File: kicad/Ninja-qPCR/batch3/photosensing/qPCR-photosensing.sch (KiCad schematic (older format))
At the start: 26 parts, among them J2 Conn_01x02_Male, J3 Conn_01x05_Male, J4 Conn_01x05_Male, U2 ADS1219IPWR

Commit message: wire xtal
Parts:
- R? (x2): value R -> ?
- Y?: value Crystal -> 32.768kHz?
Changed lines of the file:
@@
 P 4650 6000
 F 0 "R?" V 4443 6000 50  0000 C CNN
-F 1 "R" V 4534 6000 50  0000 C CNN
+F 1 "?" V 4534 6000 50  0000 C CNN
 F 2 "" V 4580 6000 50  0001 C CNN
 F 3 "~" H 4650 6000 50  0001 C CNN
@@
 P 5050 6250
 F 0 "R?" H 5120 6296 50  0000 L CNN
-F 1 "R" H 5120 6205 50  0000 L CNN
+F 1 "?" H 5120 6205 50  0000 L CNN
 F 2 "" V 4980 6250 50  0001 C CNN
 F 3 "~" H 5050 6250 50  0001 C CNN
@@
 P 4650 6500
 F 0 "Y?" H 4650 6768 50  0000 C CNN
-F 1 "Crystal" H 4650 6677 50  0000 C CNN
+F 1 "32.768kHz?" H 4650 6677 50  0000 C CNN
 F 2 "" H 4650 6500 50  0001 C CNN
 F 3 "~" H 4650 6500 50  0001 C CNN

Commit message: wire xtal
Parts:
- C? (x2): value C -> ?
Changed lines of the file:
@@
 P 4300 6750
 F 0 "C?" H 4415 6796 50  0000 L CNN
-F 1 "C" H 4415 6705 50  0000 L CNN
+F 1 "?" H 4415 6705 50  0000 L CNN
 F 2 "" H 4338 6600 50  0001 C CNN
 F 3 "~" H 4300 6750 50  0001 C CNN
@@
 P 5050 6750
 F 0 "C?" H 5165 6796 50  0000 L CNN
-F 1 "C" H 5165 6705 50  0000 L CNN
+F 1 "?" H 5165 6705 50  0000 L CNN
 F 2 "" H 5088 6600 50  0001 C CNN
 F 3 "~" H 5050 6750 50  0001 C CNN

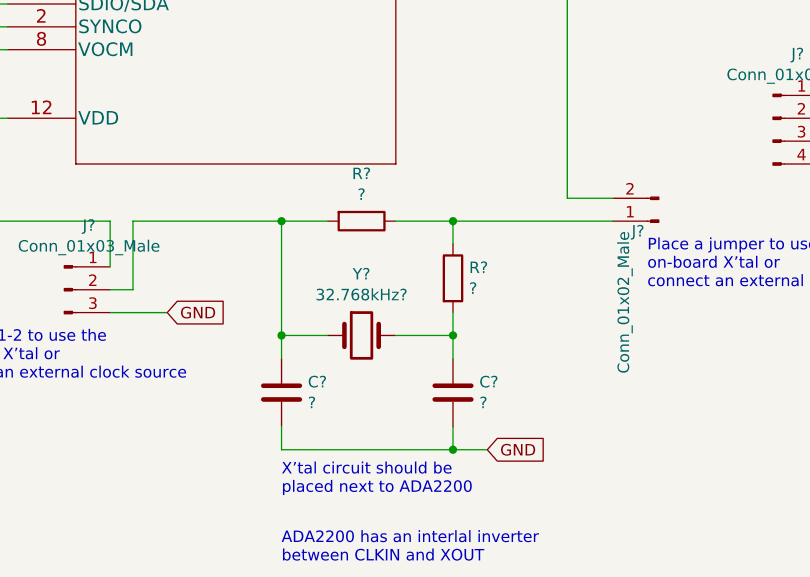
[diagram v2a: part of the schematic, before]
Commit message: change 20M to 10M+10M
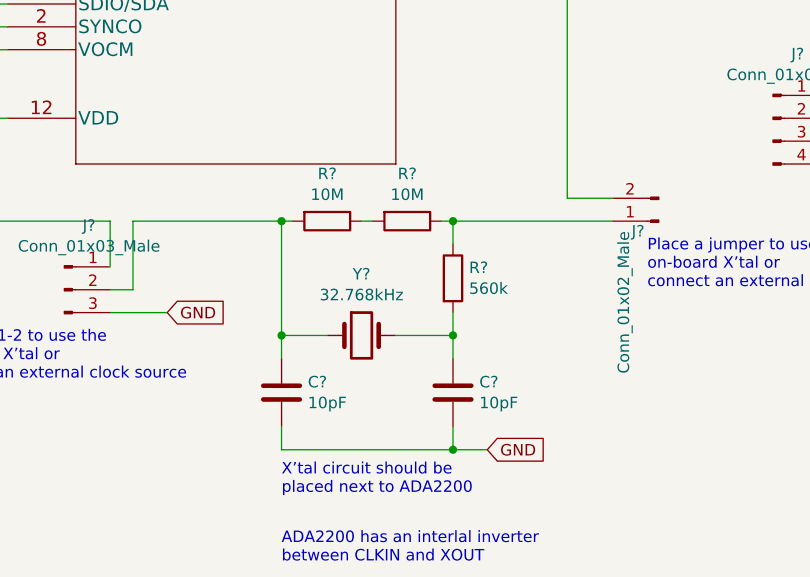
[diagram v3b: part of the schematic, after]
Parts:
- added R?: 10M, symbol Device:R
- C? (x2): value ? -> 10pF
- R?: value ? -> 10M
- R?: value ? -> 560k
- Y?: value 32.768kHz? -> 32.768kHz
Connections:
- net at J?.1 (Pin_1), R?.1: now also R?.1; no longer R?.1
- new net: R?.1, R?.2
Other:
- moved on the sheet: R?
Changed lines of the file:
@@
 L Device:R R?
 U 1 1 5FE4E4E3
-P 4650 6000
-F 0 "R?" V 4443 6000 50  0000 C CNN
-F 1 "?" V 4534 6000 50  0000 C CNN
-F 2 "" V 4580 6000 50  0001 C CNN
-F 3 "~" H 4650 6000 50  0001 C CNN
-	1    4650 6000
-	0    1    1    0
-$EndComp
-Wire Wire Line
-	4800 6000 5050 6000
-Wire Wire Line
-	4500 6000 4300 6000
+P 4500 6000
+F 0 "R?" V 4293 6000 50  0000 C CNN
+F 1 "10M" V 4384 6000 50  0000 C CNN
+F 2 "" V 4430 6000 50  0001 C CNN
+F 3 "~" H 4500 6000 50  0001 C CNN
+	1    4500 6000
+	0    1    1    0
+$EndComp
 $Comp
 L Device:R R?
@@
 P 5050 6250
 F 0 "R?" H 5120 6296 50  0000 L CNN
-F 1 "?" H 5120 6205 50  0000 L CNN
+F 1 "560k" H 5120 6205 50  0000 L CNN
 F 2 "" V 4980 6250 50  0001 C CNN
 F 3 "~" H 5050 6250 50  0001 C CNN
@@
 Wire Wire Line
 	5050 6100 5050 6000
-Connection ~ 5050 6000
 $Comp
 L Device:Crystal Y?
@@
 P 4650 6500
 F 0 "Y?" H 4650 6768 50  0000 C CNN
-F 1 "32.768kHz?" H 4650 6677 50  0000 C CNN
+F 1 "32.768kHz" H 4650 6677 50  0000 C CNN
 F 2 "" H 4650 6500 50  0001 C CNN
 F 3 "~" H 4650 6500 50  0001 C CNN
@@
 P 4300 6750
 F 0 "C?" H 4415 6796 50  0000 L CNN
-F 1 "?" H 4415 6705 50  0000 L CNN
+F 1 "10pF" H 4415 6705 50  0000 L CNN
 F 2 "" H 4338 6600 50  0001 C CNN
 F 3 "~" H 4300 6750 50  0001 C CNN
@@
 P 5050 6750
 F 0 "C?" H 5165 6796 50  0000 L CNN
-F 1 "?" H 5165 6705 50  0000 L CNN
+F 1 "10pF" H 5165 6705 50  0000 L CNN
 F 2 "" H 5088 6600 50  0001 C CNN
 F 3 "~" H 5050 6750 50  0001 C CNN
@@
 Wire Wire Line
 	3650 6000 4300 6000
-Connection ~ 4300 6000
 Wire Wire Line
 	3550 6000 2300 6000
@@
 Text Notes 6600 950  0    50   ~ 0
 SMALL GAIN FOR\nSTRONG SIGNAL
+$Comp
+L Device:R R?
+U 1 1 5FF71CFB
+P 4850 6000
+F 0 "R?" V 4643 6000 50  0000 C CNN
+F 1 "10M" V 4734 6000 50  0000 C CNN
+F 2 "" V 4780 6000 50  0001 C CNN
+F 3 "~" H 4850 6000 50  0001 C CNN
+	1    4850 6000
+	0    1    1    0
+$EndComp
+Wire Wire Line
+	5050 6000 5000 6000
+Connection ~ 5050 6000
+Wire Wire Line
+	4700 6000 4650 6000
+Wire Wire Line
+	4350 6000 4300 6000
+Connection ~ 4300 6000
 $EndSCHEMATC

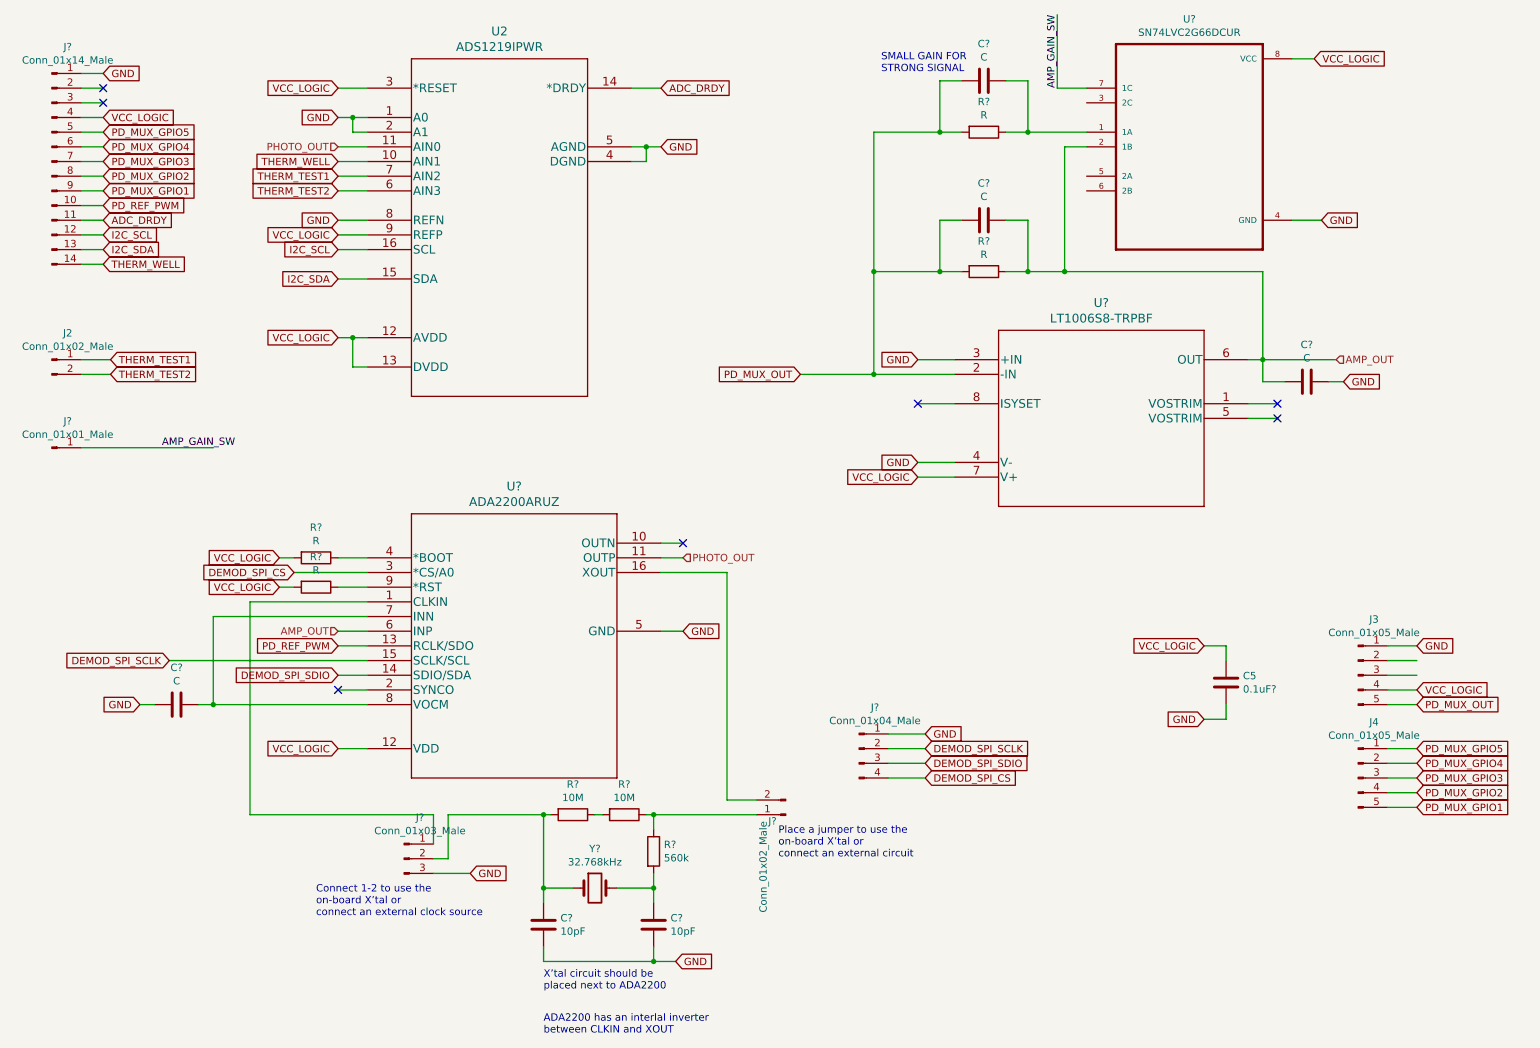
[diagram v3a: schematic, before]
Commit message: Updated values of resistor & capacitors of photosensing board
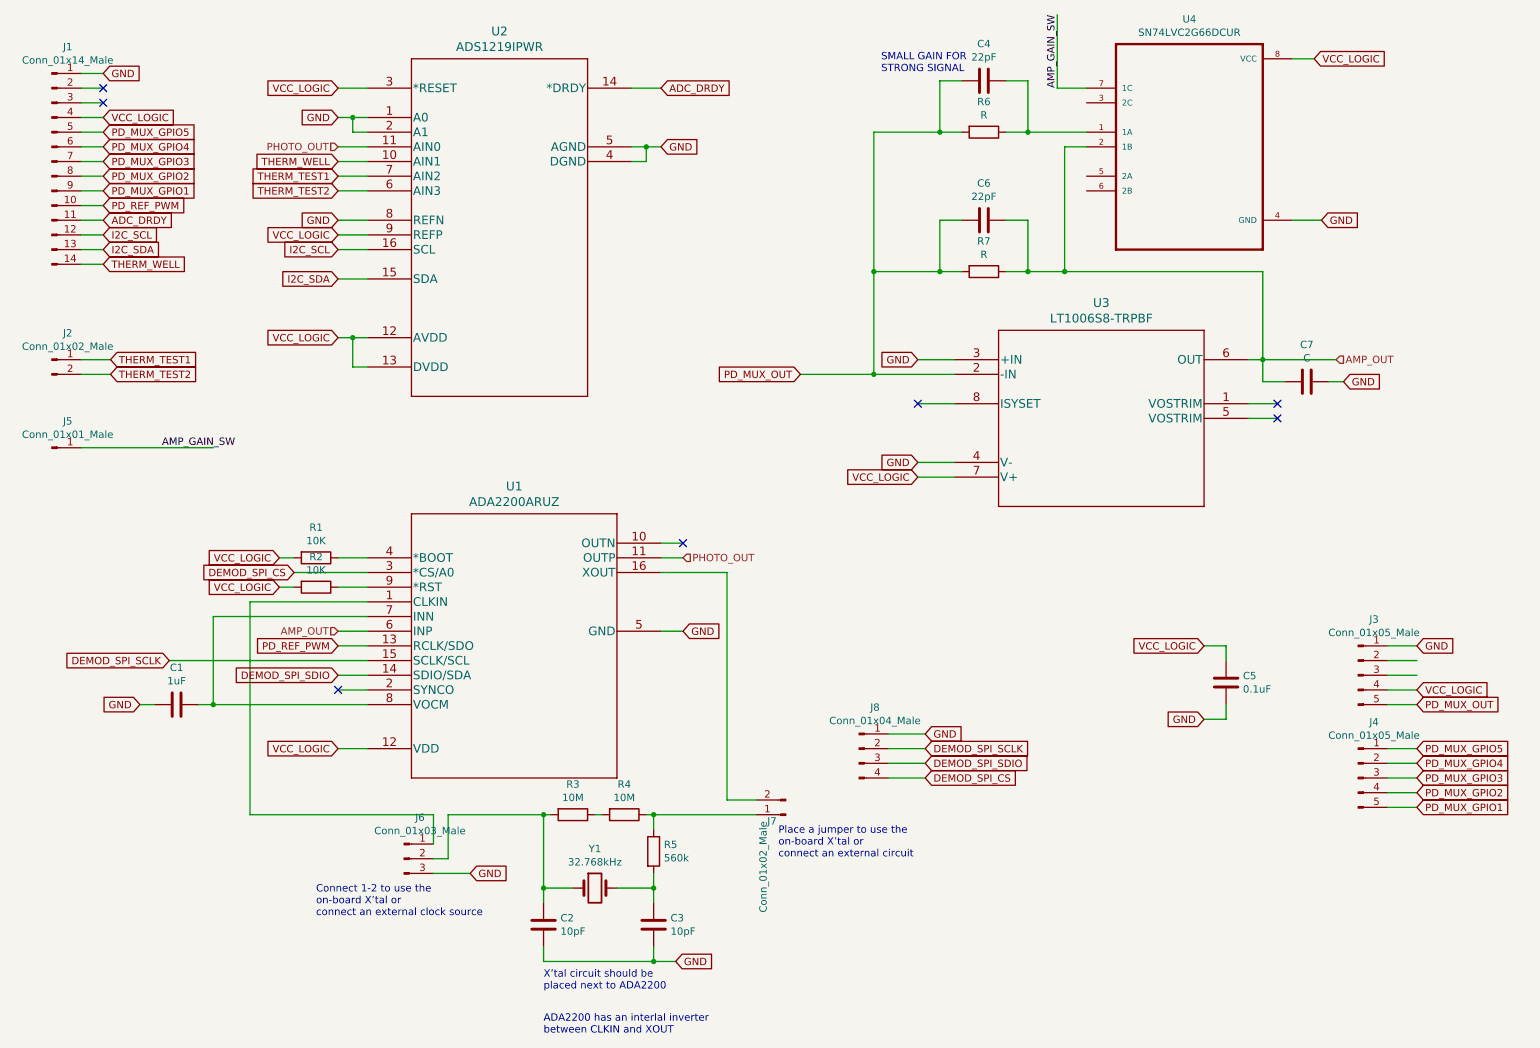
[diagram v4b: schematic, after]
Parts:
- C1: renamed from C?; value C -> 1uF
- C4, C6: renamed from C?; value C -> 22pF
- C5: value 0.1uF? -> 0.1uF
- R1, R2: renamed from R?; value R -> 10K
- gave numbers to parts that had none: 17
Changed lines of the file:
@@
 P 8950 5100
 F 0 "C5" H 9065 5146 50  0000 L CNN
-F 1 "0.1uF?" H 9065 5055 50  0000 L CNN
+F 1 "0.1uF" H 9065 5055 50  0000 L CNN
 F 2 "Capacitors_SMD:C_0805_HandSoldering" H 8988 4950 50  0001 C CNN
 F 3 "~" H 8950 5100 50  0001 C CNN
@@
 	2900 4850 3100 4850
 $Comp
-L Ninja-qPCR:ADA2200ARUZ U?
+L Ninja-qPCR:ADA2200ARUZ U1
 U 1 1 5F7FB45A
 P 3100 4250
-F 0 "U?" H 4100 4737 60  0000 C CNN
+F 0 "U1" H 4100 4737 60  0000 C CNN
 F 1 "ADA2200ARUZ" H 4100 4631 60  0000 C CNN
 F 2 "RU_16_ADI" H 4100 4590 60  0001 C CNN
@@
 $EndComp
 $Comp
-L Device:R R?
+L Device:R R1
 U 1 1 5FDD9D62
 P 2750 4250
-F 0 "R?" V 2543 4250 50  0000 C CNN
-F 1 "R" V 2634 4250 50  0000 C CNN
+F 0 "R1" V 2543 4250 50  0000 C CNN
+F 1 "10K" V 2634 4250 50  0000 C CNN
 F 2 "" V 2680 4250 50  0001 C CNN
 F 3 "~" H 2750 4250 50  0001 C CNN
@@
 $EndComp
 $Comp
-L Device:R R?
+L Device:R R2
 U 1 1 5FDDE2F4
 P 2750 4450
-F 0 "R?" V 2543 4450 50  0000 C CNN
-F 1 "R" V 2634 4450 50  0000 C CNN
+F 0 "R2" V 2543 4450 50  0000 C CNN
+F 1 "10K" V 2634 4450 50  0000 C CNN
 F 2 "" V 2680 4450 50  0001 C CNN
 F 3 "~" H 2750 4450 50  0001 C CNN
@@
 	5100 4350 5550 4350
 $Comp
-L Device:R R?
+L Device:R R3
 U 1 1 5FE4E4E3
 P 4500 6000
-F 0 "R?" V 4293 6000 50  0000 C CNN
+F 0 "R3" V 4293 6000 50  0000 C CNN
 F 1 "10M" V 4384 6000 50  0000 C CNN
 F 2 "" V 4430 6000 50  0001 C CNN
@@
 $EndComp
 $Comp
-L Device:R R?
+L Device:R R5
 U 1 1 5FE5F208
 P 5050 6250
-F 0 "R?" H 5120 6296 50  0000 L CNN
+F 0 "R5" H 5120 6296 50  0000 L CNN
 F 1 "560k" H 5120 6205 50  0000 L CNN
 F 2 "" V 4980 6250 50  0001 C CNN
@@
 	5050 6100 5050 6000
 $Comp
-L Device:Crystal Y?
+L Device:Crystal Y1
 U 1 1 5FE652B7
 P 4650 6500
-F 0 "Y?" H 4650 6768 50  0000 C CNN
+F 0 "Y1" H 4650 6768 50  0000 C CNN
 F 1 "32.768kHz" H 4650 6677 50  0000 C CNN
 F 2 "" H 4650 6500 50  0001 C CNN
@@
 	4300 6500 4300 6000
 $Comp
-L Device:C C?
+L Device:C C2
 U 1 1 5FE71967
 P 4300 6750
-F 0 "C?" H 4415 6796 50  0000 L CNN
+F 0 "C2" H 4415 6796 50  0000 L CNN
 F 1 "10pF" H 4415 6705 50  0000 L CNN
 F 2 "" H 4338 6600 50  0001 C CNN
@@
 $EndComp
 $Comp
-L Device:C C?
+L Device:C C3
 U 1 1 5FE721BD
 P 5050 6750
-F 0 "C?" H 5165 6796 50  0000 L CNN
+F 0 "C3" H 5165 6796 50  0000 L CNN
 F 1 "10pF" H 5165 6705 50  0000 L CNN
 F 2 "" H 5088 6600 50  0001 C CNN
@@
 AMP_OUT
 $Comp
-L qPCR-photosensing-rescue:LT1006S8-TRPBF-2020-12-17_04-24-35 U?
+L qPCR-photosensing-rescue:LT1006S8-TRPBF-2020-12-17_04-24-35 U3
 U 1 1 5FDCF8FF
 P 7100 2900
-F 0 "U?" H 8100 3287 60  0000 C CNN
+F 0 "U3" H 8100 3287 60  0000 C CNN
 F 1 "LT1006S8-TRPBF" H 8100 3181 60  0000 C CNN
 F 2 "SO-8_S_LIT" H 8100 3140 60  0001 C CNN
@@
 	7100 3000 6550 3000
 $Comp
-L Device:R R?
+L Device:R R7
 U 1 1 5FDF4248
 P 7300 2300
-F 0 "R?" V 7093 2300 50  0000 C CNN
+F 0 "R7" V 7093 2300 50  0000 C CNN
 F 1 "R" V 7184 2300 50  0000 C CNN
 F 2 "" V 7230 2300 50  0001 C CNN
@@
 	2050 5250 3100 5250
 $Comp
-L Device:C C?
+L Device:C C1
 U 1 1 5FDB9DB9
 P 1800 5250
-F 0 "C?" V 1548 5250 50  0000 C CNN
-F 1 "C" V 1639 5250 50  0000 C CNN
+F 0 "C1" V 1548 5250 50  0000 C CNN
+F 1 "1uF" V 1639 5250 50  0000 C CNN
 F 2 "" H 1838 5100 50  0001 C CNN
 F 3 "~" H 1800 5250 50  0001 C CNN
@@
 NoConn ~ 5250 4150
 $Comp
-L Device:C C?
+L Device:C C6
 U 1 1 5FDD2096
 P 7300 1950
-F 0 "C?" V 7048 1950 50  0000 C CNN
-F 1 "C" V 7139 1950 50  0000 C CNN
+F 0 "C6" V 7048 1950 50  0000 C CNN
+F 1 "22pF" V 7139 1950 50  0000 C CNN
 F 2 "" H 7338 1800 50  0001 C CNN
 F 3 "~" H 7300 1950 50  0001 C CNN
@@
 	7000 1950 7000 2300
 $Comp
-L Device:C C?
+L Device:C C7
 U 1 1 5FDE1D78
 P 9500 3050
-F 0 "C?" V 9248 3050 50  0000 C CNN
+F 0 "C7" V 9248 3050 50  0000 C CNN
 F 1 "C" V 9339 3050 50  0000 C CNN
 F 2 "" H 9538 2900 50  0001 C CNN
@@
 X’tal circuit should be\nplaced next to ADA2200
 $Comp
-L Connector:Conn_01x14_Male J?
+L Connector:Conn_01x14_Male J1
 U 1 1 5FDCE564
 P 950 1550
-F 0 "J?" H 1058 2331 50  0000 C CNN
+F 0 "J1" H 1058 2331 50  0000 C CNN
 F 1 "Conn_01x14_Male" H 1058 2240 50  0000 C CNN
 F 2 "" H 950 1550 50  0001 C CNN
@@
 $EndComp
 $Comp
-L Connector:Conn_01x04_Male J?
+L Connector:Conn_01x04_Male J8
 U 1 1 5FDD1B56
 P 6450 5550
-F 0 "J?" H 6558 5831 50  0000 C CNN
+F 0 "J8" H 6558 5831 50  0000 C CNN
 F 1 "Conn_01x04_Male" H 6558 5740 50  0000 C CNN
 F 2 "" H 6450 5550 50  0001 C CNN
@@
 NoConn ~ 1300 1150
 $Comp
-L Connector:Conn_01x03_Male J?
+L Connector:Conn_01x03_Male J6
 U 1 1 5FDD8186
 P 3350 6300
-F 0 "J?" H 3458 6581 50  0000 C CNN
+F 0 "J6" H 3458 6581 50  0000 C CNN
 F 1 "Conn_01x03_Male" H 3458 6490 50  0000 C CNN
 F 2 "" H 3350 6300 50  0001 C CNN
@@
 	3800 6400 3550 6400
 $Comp
-L Connector:Conn_01x02_Male J?
+L Connector:Conn_01x02_Male J7
 U 1 1 5FDECF86
 P 5950 6000
-F 0 "J?" H 6012 6044 50  0000 L CNN
+F 0 "J7" H 6012 6044 50  0000 L CNN
 F 1 "Conn_01x02_Male" V 6103 6044 50  0000 L CNN
 F 2 "" H 5950 6000 50  0001 C CNN
@@
 PD_MUX_OUT
 $Comp
-L Device:R R?
+L Device:R R6
 U 1 1 5FE329AB
 P 7300 1350
-F 0 "R?" V 7093 1350 50  0000 C CNN
+F 0 "R6" V 7093 1350 50  0000 C CNN
 F 1 "R" V 7184 1350 50  0000 C CNN
 F 2 "" V 7230 1350 50  0001 C CNN
@@
 	7150 1350 7000 1350
 $Comp
-L Device:C C?
+L Device:C C4
 U 1 1 5FE329B3
 P 7300 1000
-F 0 "C?" V 7048 1000 50  0000 C CNN
-F 1 "C" V 7139 1000 50  0000 C CNN
+F 0 "C4" V 7048 1000 50  0000 C CNN
+F 1 "22pF" V 7139 1000 50  0000 C CNN
 F 2 "" H 7338 850 50  0001 C CNN
 F 3 "~" H 7300 1000 50  0001 C CNN
@@
 	6550 2300 6550 3000
 $Comp
-L Ninja-qPCR:SN74LVC2G66DCUR U?
+L Ninja-qPCR:SN74LVC2G66DCUR U4
 U 1 1 5FE7A9A2
 P 8700 1450
-F 0 "U?" H 8700 2320 50  0000 C CNN
+F 0 "U4" H 8700 2320 50  0000 C CNN
 F 1 "SN74LVC2G66DCUR" H 8700 2229 50  0000 C CNN
 F 2 "SOP50P310X90-8N" H 8700 1450 50  0001 L BNN
@@
 AMP_GAIN_SW
 $Comp
-L Connector:Conn_01x01_Male J?
+L Connector:Conn_01x01_Male J5
 U 1 1 5FEE9D72
 P 950 3500
-F 0 "J?" H 1058 3681 50  0000 C CNN
+F 0 "J5" H 1058 3681 50  0000 C CNN
 F 1 "Conn_01x01_Male" H 1058 3590 50  0000 C CNN
 F 2 "" H 950 3500 50  0001 C CNN
@@
 SMALL GAIN FOR\nSTRONG SIGNAL
 $Comp
-L Device:R R?
+L Device:R R4
 U 1 1 5FF71CFB
 P 4850 6000
-F 0 "R?" V 4643 6000 50  0000 C CNN
+F 0 "R4" V 4643 6000 50  0000 C CNN
 F 1 "10M" V 4734 6000 50  0000 C CNN
 F 2 "" V 4780 6000 50  0001 C CNN
